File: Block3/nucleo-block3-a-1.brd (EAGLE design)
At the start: 100.3 x 80 mm, 21 parts, among them J1 DSUB-9-RIGHT-ANGLE, J2 DSUB-9-RIGHT-ANGLE, J3 DSUB-9-RIGHT-ANGLE, U1 TC4428ACOA, U2 TC4428ACOA, U3 TC4428ACOA

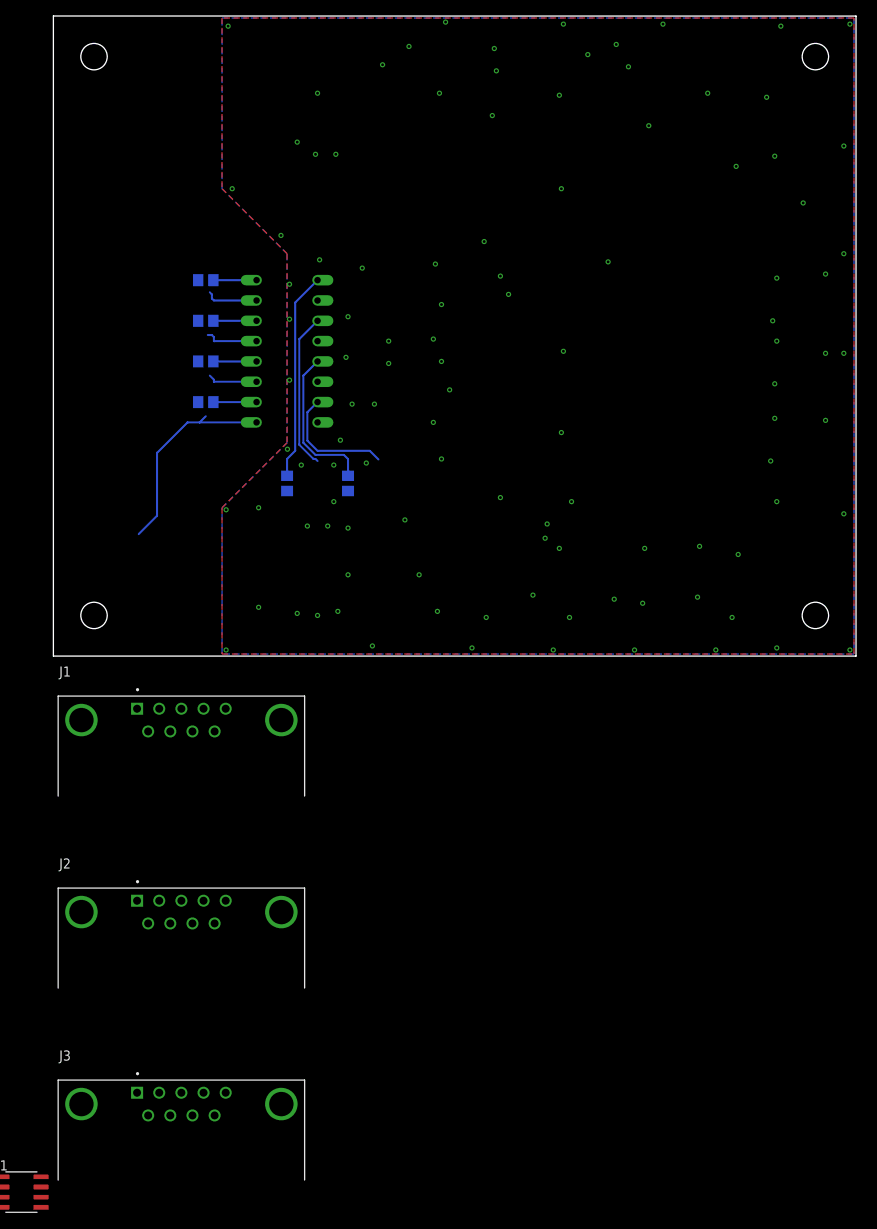
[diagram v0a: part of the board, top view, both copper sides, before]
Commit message: Adds morpho header. Lays out connectors.
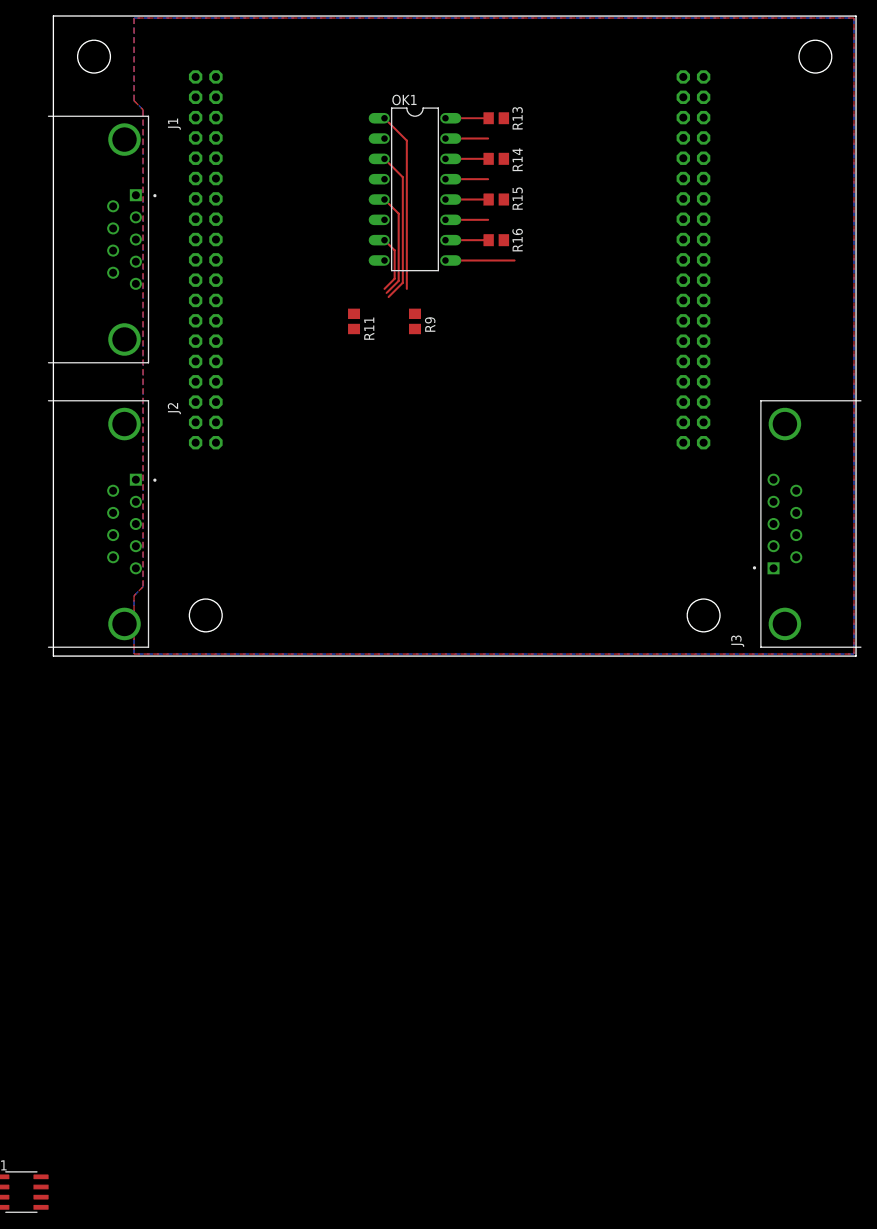
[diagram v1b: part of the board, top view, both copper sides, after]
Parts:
- added G1: NUCLEO_64_GENERIC, eagleparts:NUCLEO_BRD_BASE64
- H1, H2, H3, H4: value MOUNT-HOLE3.3 -> MOUNT-HOLE4.1; device holes:3,3 -> holes:4,1
- moved J3 104.6 mm to (91.4, 16.5), turned to 90 degrees
- moved J1 60.5 mm to (8.89, 52.1), turned to 270 degrees
- moved J2 49.0 mm to (8.89, 16.5), turned to 270 degrees
- moved R13 41.6 mm to (55.4, 67.2), flipped to the top
- moved R14 41.6 mm to (55.4, 62.1), flipped to the top
- moved R15 41.6 mm to (55.4, 57.1), flipped to the top
- moved R16 41.6 mm to (55.4, 52.0), flipped to the top
- moved OK1 25.8 mm to (45.2, 58.3), flipped to the top
- moved R9 25.8 mm to (45.2, 41.8), flipped to the top
- moved R11 20.3 mm to (37.6, 41.8), flipped to the top
- moved H2 14.0 mm to (19.1, 5.08)
- moved H3 14.0 mm to (81.3, 5.08)
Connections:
- new net 3V3: G1.3V3
- new net 5V2: G1.5V2
- new net AVDD: G1.AVDD
- new net E5V: G1.E5V
- new net GND3: G1.GND3
- new net GND6: G1.GND6
- new net GND7: G1.GND7
- new net U5V: G1.U5V
- new net VBAT: G1.VBAT
- new net VDD: G1.VDD
- new net VIN2: G1.VIN2
- net BLKA-RX: now also G1.PC11
- net BLKA-TX: now also G1.PC10
- net BLKB-RX: now also G1.PD2
- net BLKB-TX: now also G1.PC12
- net BLKC-RX: now also G1.NC6-PB11
- net BLKC-TX: now also G1.PB10
- net GND: now also G1.AGND, G1.GND4, G1.GND5, G1.GND8
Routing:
- net GND: track 45.8 -> 24.6 mm, vias 109 -> 0
- net BLKB-RX-: track 15.2 -> 7.15 mm
- net N$35: track 19.4 -> 13.1 mm
- net N$31: track 26.0 -> 22.5 mm
- net BLKA-RX-: track 19.6 -> 19.0 mm
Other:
- board text removed: "+12V"
- board text removed: "F1"
- board text removed: "F2"
- board text removed: "Farben nach 568B"
- board text removed: "GND"
- board text removed: "H"
- board text removed: "IO board nach oben"
- board text removed: "NH"
- board text removed: "NH RM"
- board text removed: "RL-F"
- board text removed: "RL-H"
- board text removed: "Rückmelder anbinden."

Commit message: Adds LN circuitry.
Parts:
- added C1: 47pF, rcl:C0805
- added D1, D2: DIODEDO-214AA-NODOC, trainlib:DO214AA-NODOC
- added J4, J5: MODJACK-6P6CCONN_SS-90000-003_STW, eagleparts:CONN_SS-90000-003_STW
- added JP1: (no value), jumper:JP1
- added Q1: NPN-23, eagleparts:SOT23
- added Q2: BSS84, eagleparts:SOT23-PCH
- added R10: 100k, rcl:R0805
- added R12, R17, R18, R19, R20, R21, R6: 47k, rcl:R0805
- added R4, R5: 12, rcl:R0805
- added R7: 1k, rcl:R0805
- added R8: DNP, rcl:R0805
- renumbered J1 to BLOCK_A, J2 to BLOCK_B, J3 to BLOCK_C
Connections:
- removed net 5V2: G1.5V2
- removed net VDD: G1.VDD
- removed net VIN2: G1.VIN2
- new net +12V: G1.VIN2, JP1.2
- new net LN-RX: R6.1
- new net LN-TX: Q2.1, R10.1
- new net N$10: Q2.3, R7.1
- new net N$11: Q1.1, R7.2, R8.1
- new net N$4: D2.A, J4.6, J5.6
- new net N$5: C1.1, R4.1, R5.2
- new net N$6: D1.A, J4.1, J5.1
- new net N$7: J4.3, J4.4, J5.3, J5.4, R4.2
- new net N$8: D1.C, D2.C, JP1.1
- new net N$9: Q1.3, R5.1, R6.2
- new net VCC: G1.VDD, Q2.2, R10.2, R12.1, R17.1, R18.1, R19.1, R20.1, R21.1
- net +5V: now also G1.5V2
- net BLKA-DET: now also R12.2
- net BLKA-RX: now also R17.2
- net BLKB-DET: now also R18.2
- net BLKB-RX: now also R19.2
- net BLKC-DET: now also R20.2
- net BLKC-RX: now also R21.2
- net GND: now also C1.2, J4.2, J4.5, J5.2, J5.5, Q1.2, R8.2

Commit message: Adds addressable LEDs.
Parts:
- added LED1, LED2, LED3, LED4, LED5, LED6, LED7, LED8, LED9: (no value), eagleparts:COM-16347_SPK-M
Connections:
- new net LED_DAT: G1.PA7, LED1.4
- new net N$12: LED1.2, LED2.4
- new net N$13: LED2.2, LED3.4
- new net N$14: LED3.2, LED4.4
- new net N$15: LED4.2, LED5.4
- new net N$16: LED5.2, LED6.4
- new net N$17: LED6.2, LED7.4
- new net N$18: LED7.2, LED8.4
- new net N$19: LED8.2, LED9.4
- net +5V: now also LED1.1, LED2.1, LED3.1, LED4.1, LED5.1, LED6.1, LED7.1, LED8.1, LED9.1
- net GND: now also LED1.3, LED2.3, LED3.3, LED4.3, LED5.3, LED6.3, LED7.3, LED8.3, LED9.3

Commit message: Places the jacks.
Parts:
- moved J5 199.3 mm to (87.6, 39.4), turned to 90 degrees
- moved J4 177.1 mm to (87.6, 57.1), turned to 90 degrees
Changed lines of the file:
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@@
 </element>
 <element name="G1" library="eagleparts" package="NUCLEO_BRD_BASE64" value="NUCLEO_64_GENERIC" x="17.78" y="26.67" smashed="yes"/>
-<element name="J4" library="eagleparts" package="CONN_SS-90000-003_STW" value="MODJACK-6P6CCONN_SS-90000-003_STW" x="-43.18" y="-62.23" smashed="yes">
-<attribute name="COPYRIGHT" value="Copyright (C) 2024 Ultra Librarian. All rights reserved." x="-43.18" y="-62.23" size="1.778" layer="27" display="off"/>
-<attribute name="MANUFACTURER_PART_NUMBER" value="SS-90000-003" x="-43.18" y="-62.23" size="1.778" layer="27" display="off"/>
-<attribute name="MFR_NAME" value="Stewart Connector" x="-43.18" y="-62.23" size="1.778" layer="27" display="off"/>
-<attribute name="NAME" x="-43.2762" y="-65.405" size="1.27" layer="27" ratio="6"/>
-<attribute name="VALUE" x="-41.7338" y="-65.405" size="1.27" layer="27" ratio="6"/>
-</element>
-<element name="J5" library="eagleparts" package="CONN_SS-90000-003_STW" value="MODJACK-6P6CCONN_SS-90000-003_STW" x="-83.82" y="-62.23" smashed="yes">
-<attribute name="COPYRIGHT" value="Copyright (C) 2024 Ultra Librarian. All rights reserved." x="-83.82" y="-62.23" size="1.778" layer="27" display="off"/>
-<attribute name="MANUFACTURER_PART_NUMBER" value="SS-90000-003" x="-83.82" y="-62.23" size="1.778" layer="27" display="off"/>
-<attribute name="MFR_NAME" value="Stewart Connector" x="-83.82" y="-62.23" size="1.778" layer="27" display="off"/>
-<attribute name="NAME" x="-83.9162" y="-65.405" size="1.27" layer="27" ratio="6"/>
-<attribute name="VALUE" x="-82.3738" y="-65.405" size="1.27" layer="27" ratio="6"/>
+<element name="J4" library="eagleparts" package="CONN_SS-90000-003_STW" value="MODJACK-6P6CCONN_SS-90000-003_STW" x="87.63" y="57.15" smashed="yes" rot="R90">
+<attribute name="COPYRIGHT" value="Copyright (C) 2024 Ultra Librarian. All rights reserved." x="87.63" y="57.15" size="1.778" layer="27" rot="R90" display="off"/>
+<attribute name="MANUFACTURER_PART_NUMBER" value="SS-90000-003" x="87.63" y="57.15" size="1.778" layer="27" rot="R90" display="off"/>
+<attribute name="MFR_NAME" value="Stewart Connector" x="87.63" y="57.15" size="1.778" layer="27" rot="R90" display="off"/>
+<attribute name="NAME" x="90.805" y="57.0538" size="1.27" layer="27" ratio="6" rot="R90"/>
+<attribute name="VALUE" x="90.805" y="58.5962" size="1.27" layer="27" ratio="6" rot="R90"/>
+</element>
+<element name="J5" library="eagleparts" package="CONN_SS-90000-003_STW" value="MODJACK-6P6CCONN_SS-90000-003_STW" x="87.63" y="39.37" smashed="yes" rot="R90">
+<attribute name="COPYRIGHT" value="Copyright (C) 2024 Ultra Librarian. All rights reserved." x="87.63" y="39.37" size="1.778" layer="27" rot="R90" display="off"/>
+<attribute name="MANUFACTURER_PART_NUMBER" value="SS-90000-003" x="87.63" y="39.37" size="1.778" layer="27" rot="R90" display="off"/>
+<attribute name="MFR_NAME" value="Stewart Connector" x="87.63" y="39.37" size="1.778" layer="27" rot="R90" display="off"/>
+<attribute name="NAME" x="90.805" y="39.2738" size="1.27" layer="27" ratio="6" rot="R90"/>
+<attribute name="VALUE" x="90.805" y="40.8162" size="1.27" layer="27" ratio="6" rot="R90"/>
 </element>
 <element name="R4" library="rcl" library_urn="urn:adsk.eagle:library:334" package="R0805" package3d_urn="urn:adsk.eagle:package:23553/2" value="12" x="-104.14" y="-101.6" smashed="yes">
@@
 <wire x1="-103.19" y1="-120.48" x2="-103.19" y2="-148.59" width="0" layer="19" extent="1-1"/>
 <wire x1="-103.19" y1="-114.3" x2="-103.19" y2="-120.48" width="0" layer="19" extent="1-1"/>
-<wire x1="-82.55" y1="-64.77" x2="-103.19" y2="-114.3" width="0" layer="19" extent="1-1"/>
-<wire x1="-78.74" y1="-62.23" x2="-82.55" y2="-64.77" width="0" layer="19" extent="1-1"/>
-<wire x1="-41.91" y1="-64.77" x2="-78.74" y2="-62.23" width="0" layer="19" extent="1-1"/>
-<wire x1="-38.1" y1="-62.23" x2="-41.91" y2="-64.77" width="0" layer="19" extent="1-1"/>
-<wire x1="-24.455" y1="-67.635" x2="-38.1" y2="-62.23" width="0" layer="19" extent="1-1"/>
+<wire x1="90.17" y1="40.64" x2="-103.19" y2="-114.3" width="0" layer="19" extent="1-1"/>
+<wire x1="87.63" y1="44.45" x2="90.17" y2="40.64" width="0" layer="19" extent="1-1"/>
+<wire x1="90.17" y1="58.42" x2="87.63" y2="44.45" width="0" layer="19" extent="1-1"/>
+<wire x1="87.63" y1="62.23" x2="90.17" y2="58.42" width="0" layer="19" extent="1-1"/>
+<wire x1="-24.455" y1="-67.635" x2="87.63" y2="62.23" width="0" layer="19" extent="1-1"/>
 <wire x1="-20.35" y1="-74.19" x2="-24.455" y2="-67.635" width="0" layer="19" extent="1-1"/>
 <wire x1="-15.27" y1="-74.19" x2="-20.35" y2="-74.19" width="0" layer="19" extent="1-1"/>
@@
 <contactref element="J4" pad="6"/>
 <contactref element="D2" pad="A"/>
-<wire x1="-36.83" y1="-64.77" x2="-77.47" y2="-64.77" width="0" layer="19" extent="1-1"/>
-<wire x1="-106.67" y1="-207.01" x2="-77.47" y2="-64.77" width="0" layer="19" extent="1-1"/>
+<wire x1="90.17" y1="63.5" x2="90.17" y2="45.72" width="0" layer="19" extent="1-1"/>
+<wire x1="-106.67" y1="-207.01" x2="90.17" y2="45.72" width="0" layer="19" extent="1-1"/>
 </signal>
 <signal name="N$6">
@@
 <contactref element="J4" pad="1"/>
 <contactref element="D1" pad="A"/>
-<wire x1="-43.18" y1="-62.23" x2="-83.82" y2="-62.23" width="0" layer="19" extent="1-1"/>
-<wire x1="-106.67" y1="-199.39" x2="-83.82" y2="-62.23" width="0" layer="19" extent="1-1"/>
+<wire x1="87.63" y1="57.15" x2="87.63" y2="39.37" width="0" layer="19" extent="1-1"/>
+<wire x1="-106.67" y1="-199.39" x2="87.63" y2="39.37" width="0" layer="19" extent="1-1"/>
 </signal>
 <signal name="N$7">
@@
 <contactref element="J5" pad="3"/>
 <contactref element="R4" pad="2"/>
-<wire x1="-80.01" y1="-64.77" x2="-103.19" y2="-101.6" width="0" layer="19" extent="1-1"/>
-<wire x1="-81.28" y1="-62.23" x2="-80.01" y2="-64.77" width="0" layer="19" extent="1-1"/>
-<wire x1="-40.64" y1="-62.23" x2="-80.01" y2="-64.77" width="0" layer="19" extent="1-1"/>
-<wire x1="-39.37" y1="-64.77" x2="-40.64" y2="-62.23" width="0" layer="19" extent="1-1"/>
+<wire x1="90.17" y1="43.18" x2="-103.19" y2="-101.6" width="0" layer="19" extent="1-1"/>
+<wire x1="87.63" y1="41.91" x2="90.17" y2="43.18" width="0" layer="19" extent="1-1"/>
+<wire x1="87.63" y1="59.69" x2="90.17" y2="43.18" width="0" layer="19" extent="1-1"/>
+<wire x1="90.17" y1="60.96" x2="87.63" y2="59.69" width="0" layer="19" extent="1-1"/>
 </signal>
 <signal name="N$5">

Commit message: Replace 6p6c jack with a different one that is smaller in size.
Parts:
- removed LED1, LED2, LED3, LED4, LED5, LED6, LED7, LED8, LED9: (no value), eagleparts:COM-16347_SPK-M
- J4, J5: value MODJACK-6P6CCONN_SS-90000-003_STW -> MODJACK6P6C-MJ3245-66-0CONN_MJ3245-66-0_GCT; device eagleparts:CONN_SS-90000-003_STW -> eagleparts:CONN_MJ3245-66-0_GCT
- moved J5 6.84 mm to (90.2, 45.7)
- moved J4 5.68 mm to (90.2, 62.2)
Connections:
- removed net LED_DAT: G1.PA7, LED1.4
- removed net N$12: LED1.2, LED2.4
- removed net N$13: LED2.2, LED3.4
- removed net N$14: LED3.2, LED4.4
- removed net N$15: LED4.2, LED5.4
- removed net N$16: LED5.2, LED6.4
- removed net N$17: LED6.2, LED7.4
- removed net N$18: LED7.2, LED8.4
- removed net N$19: LED8.2, LED9.4
- net +5V: no longer LED1.1, LED2.1, LED3.1, LED4.1, LED5.1, LED6.1, LED7.1, LED8.1, LED9.1
- net GND: no longer LED1.3, LED2.3, LED3.3, LED4.3, LED5.3, LED6.3, LED7.3, LED8.3, LED9.3
